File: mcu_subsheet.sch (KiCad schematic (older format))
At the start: 0 parts

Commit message: [MCU]: mcu update
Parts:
- added C?: C_Small, symbol Device:C_Small
- added U?: STM32F107RCTx, Package_QFP:LQFP-64_10x10mm_P0.5mm, symbol MCU_ST_STM32F1:STM32F107RCTx
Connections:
- net NRST: now also C?.2, U?.7 (NRST)
- net RMII_CRS_DV: now also U?.23 (PA7)
- net RMII_MDC: now also U?.9 (PC1)
- net RMII_MDIO: now also U?.16 (PA2)
- net RMII_REF_CLK: now also U?.15 (PA1)
- net RMII_RXD0: now also U?.24 (PC4)
- net RMII_RXD1: now also U?.25 (PC5)
- net RMII_TXD0: now also U?.33 (PB12)
- net RMII_TXD1: now also U?.34 (PB13)
- net RMII_TX_EN: now also U?.30 (PB11)
- new net +3V3: U?.1 (VBAT), U?.13 (VDDA), U?.19 (VDD), U?.32 (VDD), U?.48 (VDD), U?.64 (VDD)
- new net Earth: C?.1, U?.12 (VSSA), U?.18 (VSS), U?.31 (VSS), U?.47 (VSS), U?.60 (BOOT0), U?.63 (VSS)
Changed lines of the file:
@@
 $Descr A4 11693 8268
 encoding utf-8
-Sheet 2 3
+Sheet 3 3
 Title ""
 Date ""
@@
 Comment4 ""
 $EndDescr
-Text HLabel 8500 3100 0    75   Output ~ 0
+Text HLabel 6275 5200 2    75   Output ~ 0
 RMII_TX_EN
-Text HLabel 8500 3300 0    75   Output ~ 0
+Text HLabel 6275 5300 2    75   Output ~ 0
 RMII_TXD0
-Text HLabel 8500 3500 0    75   Output ~ 0
+Text HLabel 6275 5400 2    75   Output ~ 0
 RMII_TXD1
-Text HLabel 8500 3700 0    75   Input ~ 0
+Text HLabel 4675 4500 0    75   Input ~ 0
 RMII_RXD0
-Text HLabel 8500 3900 0    75   Input ~ 0
+Text HLabel 4675 4600 0    75   Input ~ 0
 RMII_RXD1
-Text HLabel 8500 4100 0    75   Input ~ 0
+Text HLabel 6275 3100 2    75   Input ~ 0
 RMII_CRS_DV
-Text HLabel 8500 4300 0    75   Output ~ 0
+Text HLabel 4675 4200 0    75   Output ~ 0
 RMII_MDC
-Text HLabel 8500 4500 0    75   BiDi ~ 0
+Text HLabel 6275 2600 2    75   BiDi ~ 0
 RMII_MDIO
-Text HLabel 8500 4700 0    75   Input ~ 0
+Text HLabel 6275 2500 2    75   Input ~ 0
 RMII_REF_CLK
 Text HLabel 8500 5300 0    75   UnSpc ~ 0
 GND
-Text HLabel 1700 5300 0    75   UnSpc ~ 0
+Text HLabel 4300 2400 0    75   UnSpc ~ 0
 NRST
 Text HLabel 1700 3000 0    75   BiDi ~ 0
@@
 Text HLabel 1700 3800 0    75   BiDi ~ 0
 PF[4..7]
+$Comp
+L MCU_ST_STM32F1:STM32F107RCTx U?
+U 1 1 61D5A186
+P 5475 4000
+F 0 "U?" H 4900 2125 50  0000 C CNN
+F 1 "STM32F107RCTx" H 5150 2025 50  0000 C CNN
+F 2 "Package_QFP:LQFP-64_10x10mm_P0.5mm" H 4875 2300 50  0001 R CNN
+F 3 "http://www.st.com/st-web-ui/static/active/en/resource/technical/document/datasheet/CD00220364.pdf" H 5475 4000 50  0001 C CNN
+	1    5475 4000
+	1    0    0    -1
+$EndComp
+Wire Wire Line
+	6175 5200 6275 5200
+Wire Wire Line
+	6175 5300 6275 5300
+Wire Wire Line
+	6175 5400 6275 5400
+Wire Wire Line
+	4675 4500 4775 4500
+Wire Wire Line
+	4675 4600 4775 4600
+Wire Wire Line
+	4675 4200 4775 4200
+Wire Wire Line
+	6175 3100 6275 3100
+Wire Wire Line
+	6175 2500 6275 2500
+Wire Wire Line
+	6175 2600 6275 2600
+$Comp
+L power:+3V3 #PWR?
+U 1 1 61D74000
+P 5175 2000
+F 0 "#PWR?" H 5175 1850 50  0001 C CNN
+F 1 "+3V3" H 5190 2173 50  0000 C CNN
+F 2 "" H 5175 2000 50  0001 C CNN
+F 3 "" H 5175 2000 50  0001 C CNN
+	1    5175 2000
+	1    0    0    -1
+$EndComp
+Wire Wire Line
+	5275 2200 5275 2100
+Wire Wire Line
+	5275 2100 5375 2100
+Wire Wire Line
+	5375 2100 5375 2200
+Wire Wire Line
+	5375 2100 5475 2100
+Wire Wire Line
+	5475 2100 5475 2200
+Connection ~ 5375 2100
+Wire Wire Line
+	5475 2100 5575 2100
+Wire Wire Line
+	5575 2100 5575 2200
+Connection ~ 5475 2100
+Wire Wire Line
+	5675 2200 5675 2100
+Wire Wire Line
+	5675 2100 5575 2100
+Connection ~ 5575 2100
+Wire Wire Line
+	5775 2200 5775 2100
+Wire Wire Line
+	5775 2100 5675 2100
+Connection ~ 5675 2100
+Wire Wire Line
+	5275 2100 5175 2100
+Wire Wire Line
+	5175 2100 5175 2000
+Connection ~ 5275 2100
+$Comp
+L Device:C_Small C?
+U 1 1 61D7B19B
+P 4400 2600
+F 0 "C?" H 4492 2646 50  0000 L CNN
+F 1 "C_Small" H 4492 2555 50  0000 L CNN
+F 2 "" H 4400 2600 50  0001 C CNN
+F 3 "~" H 4400 2600 50  0001 C CNN
+	1    4400 2600
+	-1   0    0    1
+$EndComp
+Wire Wire Line
+	4400 2500 4400 2400
+Wire Wire Line
+	4400 2400 4775 2400
+$Comp
+L power:Earth #PWR?
+U 1 1 61D7EBFD
+P 4400 2800
+F 0 "#PWR?" H 4400 2550 50  0001 C CNN
+F 1 "Earth" H 4400 2650 50  0001 C CNN
+F 2 "" H 4400 2800 50  0001 C CNN
+F 3 "~" H 4400 2800 50  0001 C CNN
+	1    4400 2800
+	1    0    0    -1
+$EndComp
+Wire Wire Line
+	4400 2800 4400 2700
+$Comp
+L power:Earth #PWR?
+U 1 1 61D80386
+P 4675 2700
+F 0 "#PWR?" H 4675 2450 50  0001 C CNN
+F 1 "Earth" H 4675 2550 50  0001 C CNN
+F 2 "" H 4675 2700 50  0001 C CNN
+F 3 "~" H 4675 2700 50  0001 C CNN
+	1    4675 2700
+	1    0    0    -1
+$EndComp
+Wire Wire Line
+	5275 5800 5275 5900
+Wire Wire Line
+	5275 5900 5375 5900
+Wire Wire Line
+	5375 5900 5375 5800
+Wire Wire Line
+	5475 5800 5475 5900
+Wire Wire Line
+	5475 5900 5375 5900
+Connection ~ 5375 5900
+Wire Wire Line
+	5475 5900 5575 5900
+Wire Wire Line
+	5575 5900 5575 5800
+Connection ~ 5475 5900
+Wire Wire Line
+	5675 5800 5675 5900
+Wire Wire Line
+	5675 5900 5575 5900
+Connection ~ 5575 5900
+Wire Wire Line
+	5675 5900 5775 5900
+Connection ~ 5675 5900
+Wire Wire Line
+	5775 5900 5775 6000
+$Comp
+L power:Earth #PWR?
+U 1 1 61D8674C
+P 5775 6000
+F 0 "#PWR?" H 5775 5750 50  0001 C CNN
+F 1 "Earth" H 5775 5850 50  0001 C CNN
+F 2 "" H 5775 6000 50  0001 C CNN
+F 3 "~" H 5775 6000 50  0001 C CNN
+	1    5775 6000
+	1    0    0    -1
+$EndComp
+Wire Wire Line
+	4675 2600 4775 2600
+Wire Wire Line
+	4675 2600 4675 2700
+Wire Wire Line
+	4300 2400 4400 2400
+Connection ~ 4400 2400
 $EndSCHEMATC

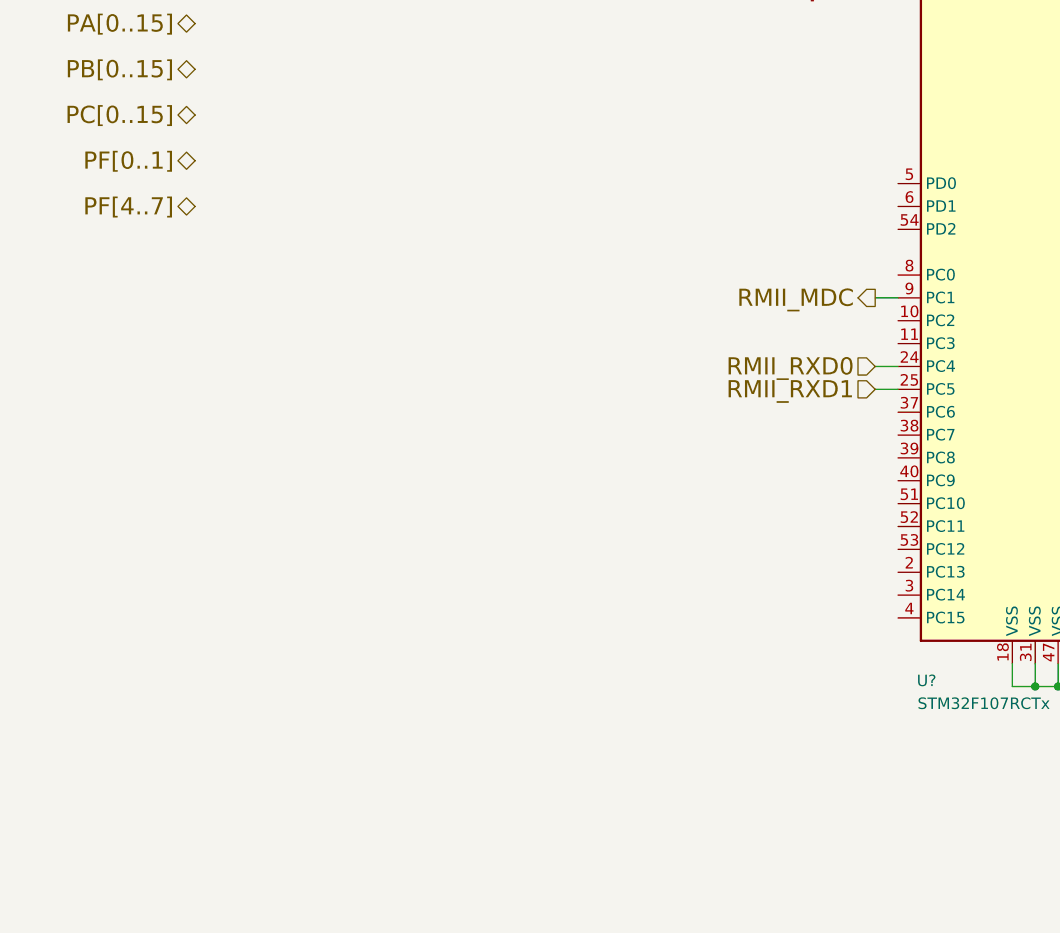
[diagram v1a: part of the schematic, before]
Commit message: [CANgate]: mcu oscillator part update
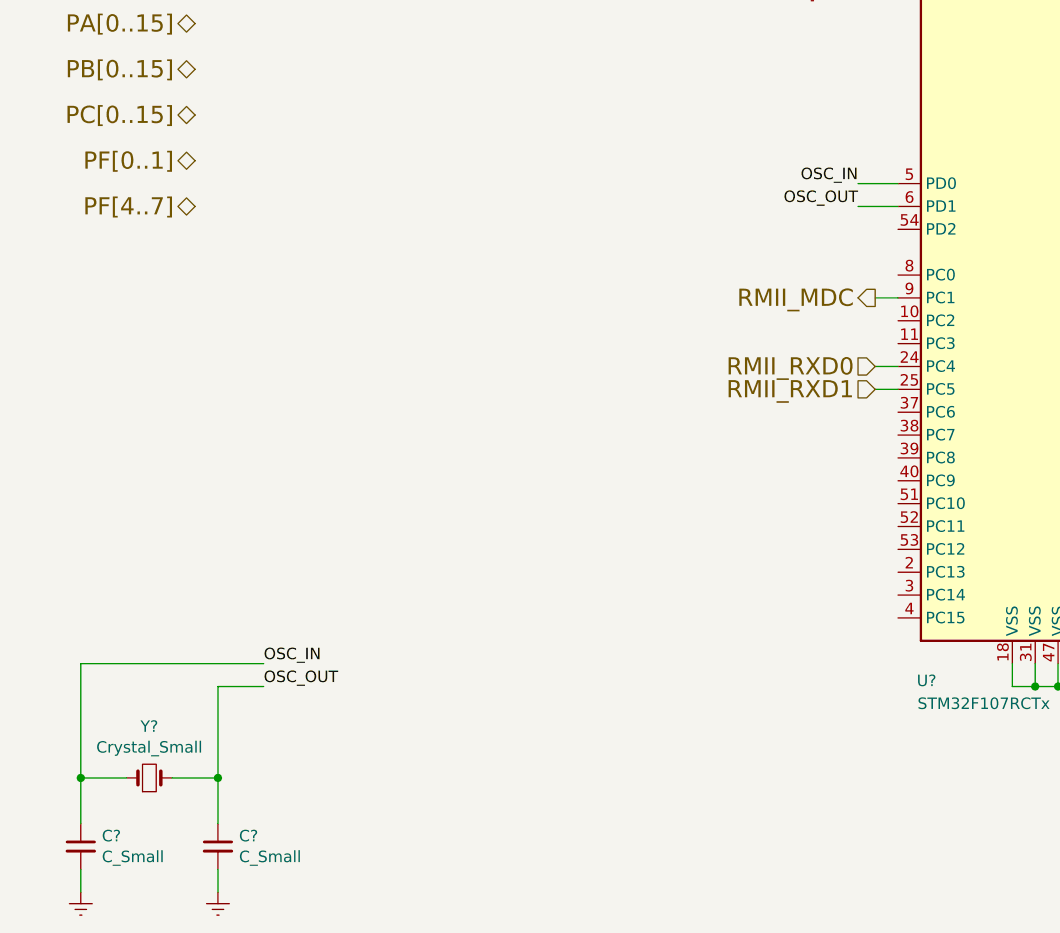
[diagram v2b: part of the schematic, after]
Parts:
- added C? (x2): C_Small, symbol Device:C_Small
- added Y?: Crystal_Small, Crystal:Crystal_SMD_Abracon_ABM3-2Pin_5.0x3.2mm_HandSoldering, symbol Device:Crystal_Small
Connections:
- net Earth: now also C?.2, C?.2
- net OSC_IN: now reaches U?.5 (PD0)
- net OSC_IN: now also C?.1, Y?.1
- net OSC_OUT: now reaches U?.6 (PD1)
- net OSC_OUT: now also C?.1, Y?.2
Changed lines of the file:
@@
 Text HLabel 1700 3800 0    75   BiDi ~ 0
 PF[4..7]
-$Comp
-L MCU_ST_STM32F1:STM32F107RCTx U?
-U 1 1 61D5A186
-P 5475 4000
-F 0 "U?" H 4900 2125 50  0000 C CNN
-F 1 "STM32F107RCTx" H 5150 2025 50  0000 C CNN
-F 2 "Package_QFP:LQFP-64_10x10mm_P0.5mm" H 4875 2300 50  0001 R CNN
-F 3 "http://www.st.com/st-web-ui/static/active/en/resource/technical/document/datasheet/CD00220364.pdf" H 5475 4000 50  0001 C CNN
-	1    5475 4000
-	1    0    0    -1
-$EndComp
 Wire Wire Line
 	6175 5200 6275 5200
@@
 	4300 2400 4400 2400
 Connection ~ 4400 2400
+$Comp
+L Device:Crystal_Small Y?
+U 1 1 61D4BE60
+P 1500 6300
+AR Path="/6176B826/61D4BE60" Ref="Y?"  Part="1"
+AR Path="/6176B761/61D4BE60" Ref="Y?"  Part="1"
+F 0 "Y?" H 1500 6525 50  0000 C CNN
+F 1 "Crystal_Small" H 1500 6434 50  0000 C CNN
+F 2 "Crystal:Crystal_SMD_Abracon_ABM3-2Pin_5.0x3.2mm_HandSoldering" H 1500 6300 50  0001 C CNN
+F 3 "~" H 1500 6300 50  0001 C CNN
+	1    1500 6300
+	1    0    0    -1
+$EndComp
+$Comp
+L Device:C_Small C?
+U 1 1 61D4BE67
+P 1200 6600
+AR Path="/6176B826/61D4BE67" Ref="C?"  Part="1"
+AR Path="/6176B761/61D4BE67" Ref="C?"  Part="1"
+F 0 "C?" H 1292 6646 50  0000 L CNN
+F 1 "C_Small" H 1292 6555 50  0000 L CNN
+F 2 "" H 1200 6600 50  0001 C CNN
+F 3 "~" H 1200 6600 50  0001 C CNN
+	1    1200 6600
+	1    0    0    -1
+$EndComp
+$Comp
+L Device:C_Small C?
+U 1 1 61D4BE6D
+P 1800 6600
+AR Path="/6176B826/61D4BE6D" Ref="C?"  Part="1"
+AR Path="/6176B761/61D4BE6D" Ref="C?"  Part="1"
+F 0 "C?" H 1892 6646 50  0000 L CNN
+F 1 "C_Small" H 1892 6555 50  0000 L CNN
+F 2 "" H 1800 6600 50  0001 C CNN
+F 3 "~" H 1800 6600 50  0001 C CNN
+	1    1800 6600
+	1    0    0    -1
+$EndComp
+$Comp
+L power:Earth #PWR?
+U 1 1 61D4BE73
+P 1200 6800
+AR Path="/6176B826/61D4BE73" Ref="#PWR?"  Part="1"
+AR Path="/6176B761/61D4BE73" Ref="#PWR?"  Part="1"
+F 0 "#PWR?" H 1200 6550 50  0001 C CNN
+F 1 "Earth" H 1200 6650 50  0001 C CNN
+F 2 "" H 1200 6800 50  0001 C CNN
+F 3 "~" H 1200 6800 50  0001 C CNN
+	1    1200 6800
+	1    0    0    -1
+$EndComp
+$Comp
+L power:Earth #PWR?
+U 1 1 61D4BE79
+P 1800 6800
+AR Path="/6176B826/61D4BE79" Ref="#PWR?"  Part="1"
+AR Path="/6176B761/61D4BE79" Ref="#PWR?"  Part="1"
+F 0 "#PWR?" H 1800 6550 50  0001 C CNN
+F 1 "Earth" H 1800 6650 50  0001 C CNN
+F 2 "" H 1800 6800 50  0001 C CNN
+F 3 "~" H 1800 6800 50  0001 C CNN
+	1    1800 6800
+	1    0    0    -1
+$EndComp
+Wire Wire Line
+	1200 6700 1200 6800
+Wire Wire Line
+	1800 6700 1800 6800
+Wire Wire Line
+	1400 6300 1200 6300
+Wire Wire Line
+	1200 6300 1200 6500
+Wire Wire Line
+	1600 6300 1800 6300
+Wire Wire Line
+	1800 6300 1800 6500
+Wire Wire Line
+	1200 6300 1200 5800
+Wire Wire Line
+	1200 5800 2000 5800
+Connection ~ 1200 6300
+Wire Wire Line
+	1800 6300 1800 5900
+Wire Wire Line
+	1800 5900 2000 5900
+Connection ~ 1800 6300
+Text Label 2000 5800 0    50   ~ 0
+OSC_IN
+Text Label 4600 3700 2    50   ~ 0
+OSC_IN
+Wire Wire Line
+	4600 3700 4775 3700
+$Comp
+L MCU_ST_STM32F1:STM32F107RCTx U?
+U 1 1 61D5A186
+P 5475 4000
+F 0 "U?" H 4900 2125 50  0000 C CNN
+F 1 "STM32F107RCTx" H 5150 2025 50  0000 C CNN
+F 2 "Package_QFP:LQFP-64_10x10mm_P0.5mm" H 4875 2300 50  0001 R CNN
+F 3 "http://www.st.com/st-web-ui/static/active/en/resource/technical/document/datasheet/CD00220364.pdf" H 5475 4000 50  0001 C CNN
+	1    5475 4000
+	1    0    0    -1
+$EndComp
+Wire Wire Line
+	4775 3800 4600 3800
+Text Label 4600 3800 2    50   ~ 0
+OSC_OUT
+Text Label 2000 5900 0    50   ~ 0
+OSC_OUT
 $EndSCHEMATC
